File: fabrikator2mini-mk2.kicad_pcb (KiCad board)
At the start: 2 copper layers, 100 x 100 mm, 118 parts, among them CON1 Micro_SD_Card, J1 USB_OTG, J10 END_X/ESP, J11 MT_Y, J12 Conn_01x12, J13 Z, J14 MT_Z, J15 B, J16 BTN1, J17 Fan1, J2 RESET, J3 PWR_IN, J4 B, J5 I2C, J6 SWD, J7 SPI, J8 Fan2, J9 MT_X, P16 SW_DIP, P17 SW_DIP, P18 SW_DIP, P19 SW_DIP, Q1 PSMN2R4-30MLD, Q2 PSMN2R4-30MLD, Q3 PSMN2R4-30MLD, Q4 PSMN2R4-30MLD, Q5 Si7145DP, U1 bluepill, U2 CPDT6-5V4, U3 CPDT6-5V4, U4 4988, U5 4988, U6 4988, U7 4988, U9 TS30011

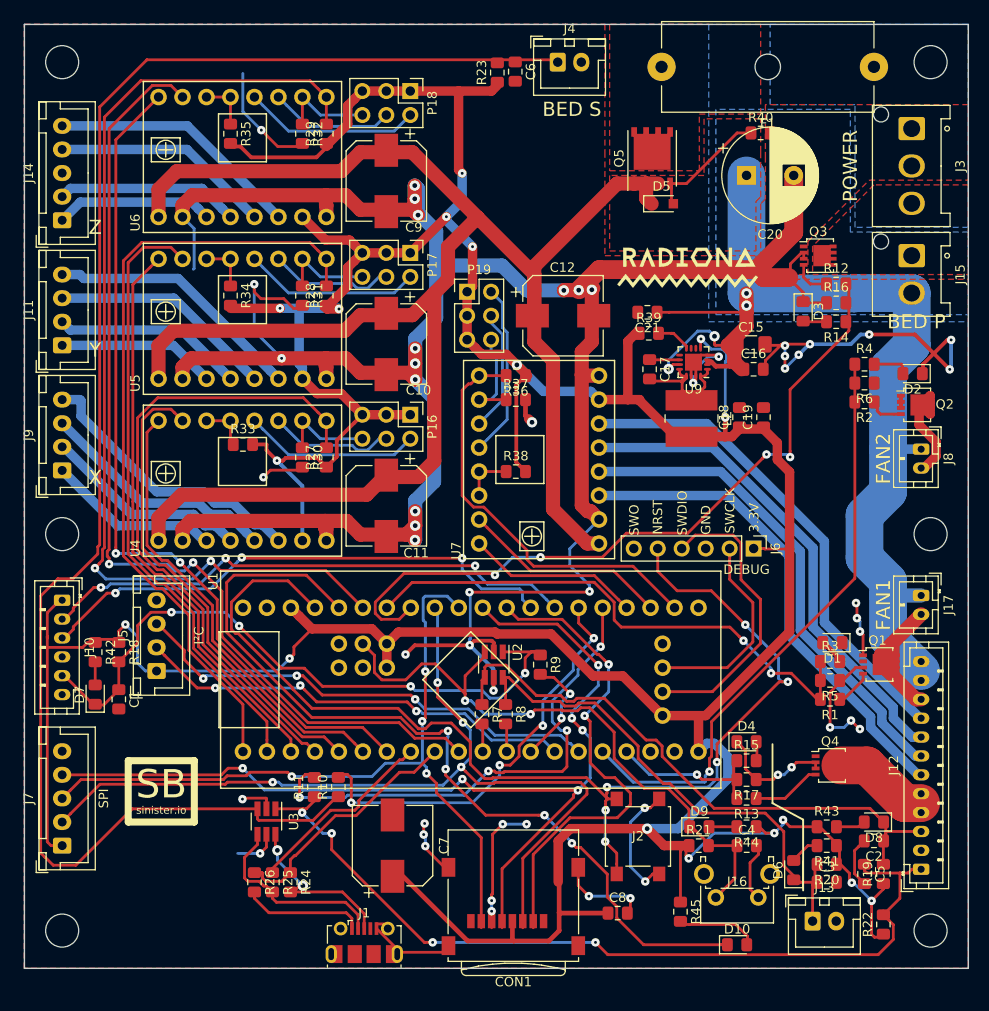
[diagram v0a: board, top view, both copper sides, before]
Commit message: silkscreen corrections
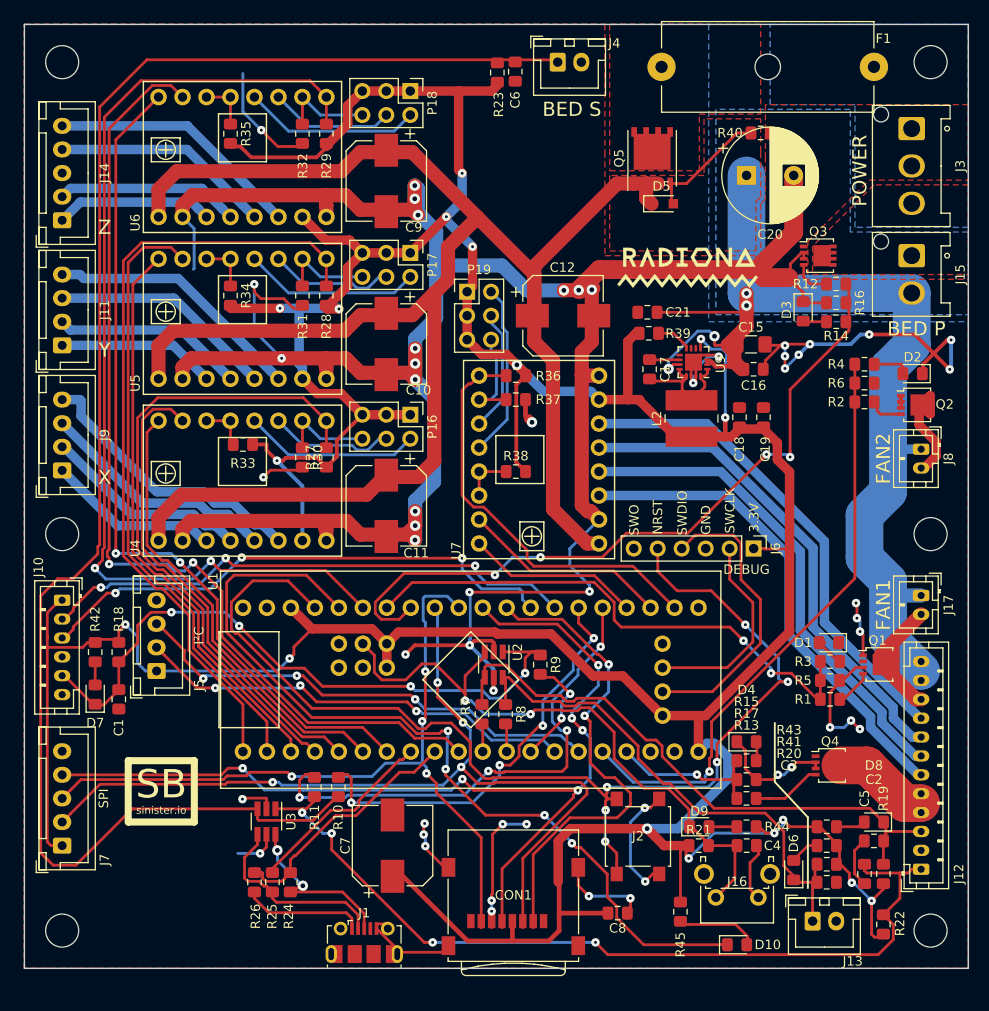
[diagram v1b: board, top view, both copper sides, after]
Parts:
- moved D1 0.38 mm to (105.2, 85.5)
